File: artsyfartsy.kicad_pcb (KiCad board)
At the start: 2 copper layers, 103.4 x 58.3 mm, 29 parts, among them J1 Conn_01x02_Male, SW1 SW_Push, SW11 SW_Push_SPDT, SW12 SW_Push_SPDT, SW2 SW_Push, SW3 SW_Push, SW4 SW_Push, SW5 SW_Push, SW6 SW_Push, SW7 SW_Push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

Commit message: encoder
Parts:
- moved SW11 37.4 mm to (113.5, 84.0), turned to 5 degrees
- moved SW12 37.4 mm to (113.5, 84.0), turned to -175 degrees
- moved J1 13.8 mm to (142.6, 66.3)
- moved SW9 6.88 mm to (143.8, 75.5)
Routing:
- net bat1: track 19.0 -> 46.4 mm, vias 0 -> 1
- net Net-(JP9-Pad2): track 46.3 -> 36.6 mm
- net so: track 63.0 -> 56.5 mm
- net Net-(JP10-Pad2): track 40.0 -> 33.7 mm, vias 0 -> 1
- net 2: track 93.4 -> 91.0 mm
- net 13: track 85.1 -> 82.7 mm
- net 9: track 129.6 -> 131.9 mm
- net 1: track 75.4 -> 73.2 mm
- net 8: track 94.5 -> 96.7 mm
- net 7: track 88.7 -> 90.6 mm
- net 4: track 127.2 -> 129.1 mm
- net Net-(JP2-Pad2): track 42.7 -> 42.0 mm
- net 14: track 69.9 -> 69.4 mm
- net GND: vias 41 -> 40

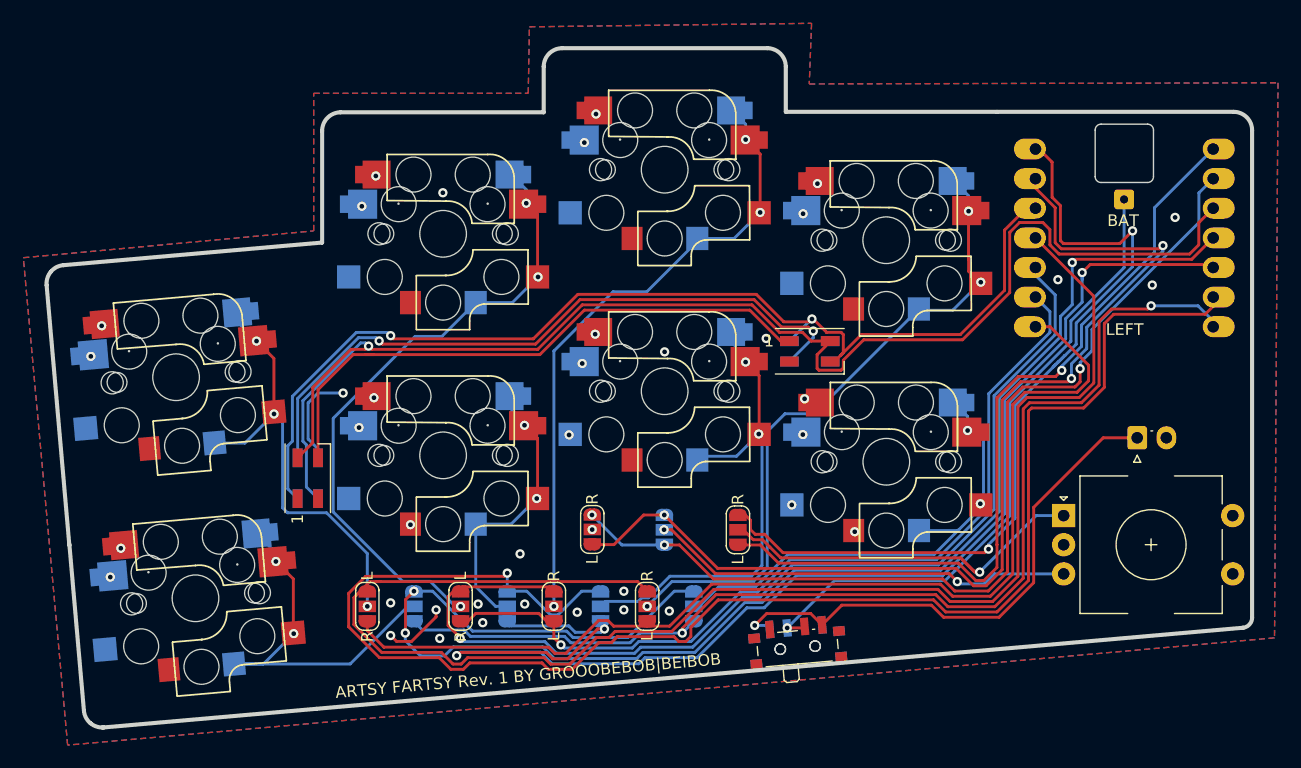
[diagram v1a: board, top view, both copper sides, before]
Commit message: updated service hole fot battery
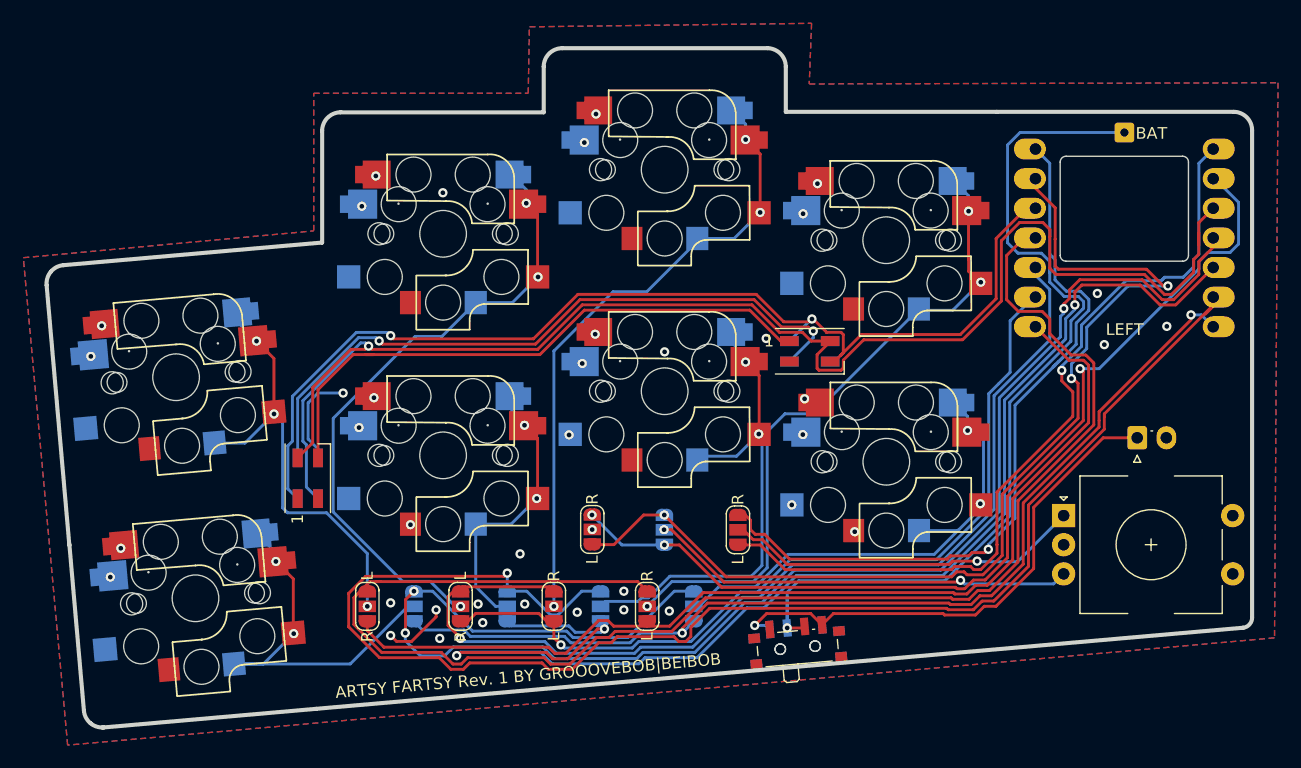
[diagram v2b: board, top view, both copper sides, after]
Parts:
- moved H1 5.74 mm to (141.5, 40.1)
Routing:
- net so: track 56.5 -> 79.7 mm
- net 8: track 96.7 -> 87.2 mm
- net 1: track 73.2 -> 66.1 mm, vias 2 -> 1
- net 9: track 131.9 -> 125.0 mm
- net VCC: track 122.6 -> 128.7 mm
- net 7: track 90.6 -> 86.5 mm
- net Net-(JP10-Pad2): track 33.7 -> 30.9 mm
- net bat1: track 46.4 -> 44.9 mm
- net 11: track 126.2 -> 127.5 mm
- net 2: track 91.0 -> 89.8 mm
- net 6: track 73.3 -> 72.4 mm
- net 13: track 82.7 -> 83.4 mm
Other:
- board text added: "ARTSY FARTSY Rev. 1 BY GROOOVEBOB|BEIBOB"
- board text removed: "ARTSY FARTSY Rev. 1 BY GROOOBEBOB|BEIBOB"

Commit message: removed sweaty palms
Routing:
- net GND: track 14.0 -> 34.8 mm, vias 40 -> 42
- net so: track 79.7 -> 75.9 mm
- net VCC: track 128.7 -> 131.2 mm, vias 1 -> 3
- net 1: track 66.1 -> 64.4 mm
- net LED: track 93.0 -> 93.6 mm
- net Net-(D1-Pad1): track 50.8 -> 50.2 mm

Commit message: update
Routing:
- net 4: track 129.2 -> 128.5 mm
- net LED: track 93.6 -> 93.1 mm
- net GND: vias 42 -> 45
